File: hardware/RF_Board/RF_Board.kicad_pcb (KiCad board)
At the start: 4 copper layers, 90 x 90 mm, 130 parts, among them J1 Conn_Coaxial, J2 Conn_01x04_Male, J3 Conn_Coaxial, J4 Conn_01x04_Male, J5 Conn_01x06_Female, J6 Conn_01x06_Female, J7 Conn_01x06_Female, J8 L77TSAH15SOL2RM8, J9 Conn_01x09_Male, Q1 2N7002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

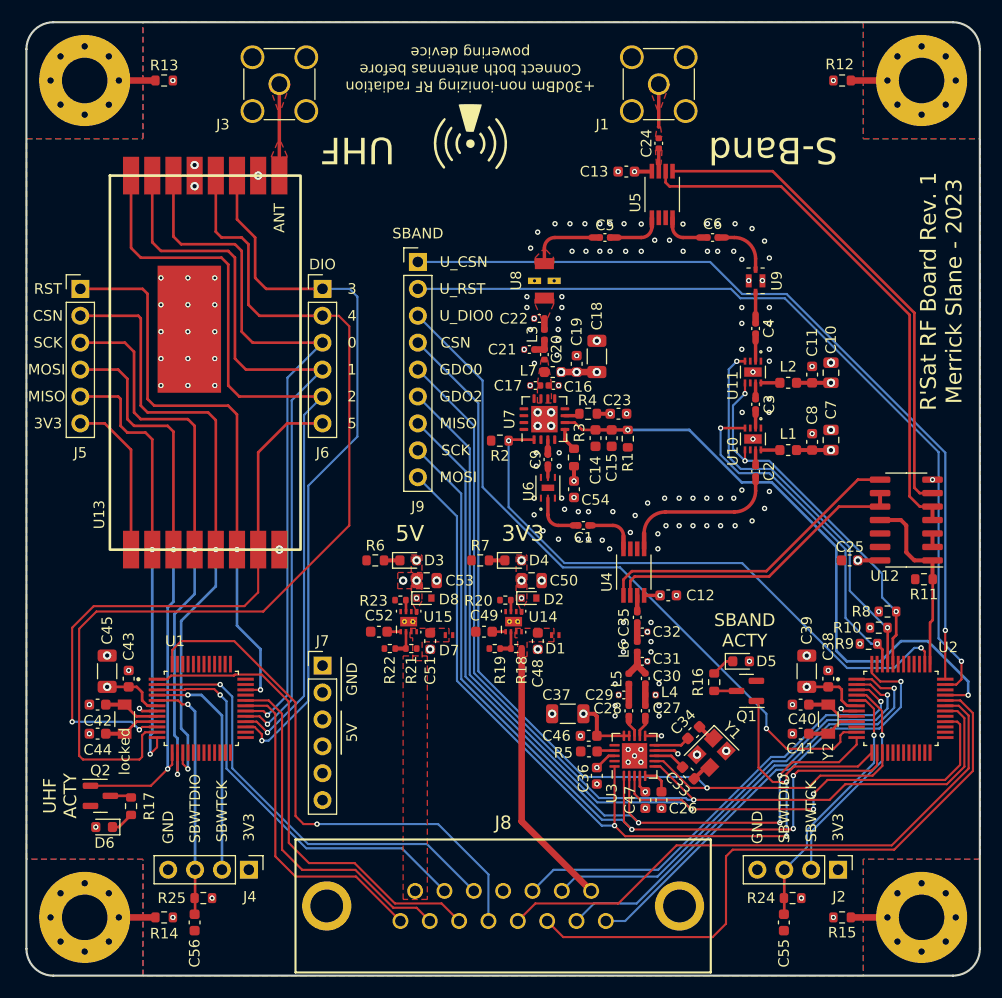
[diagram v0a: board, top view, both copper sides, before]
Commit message: respond to RF board feedback
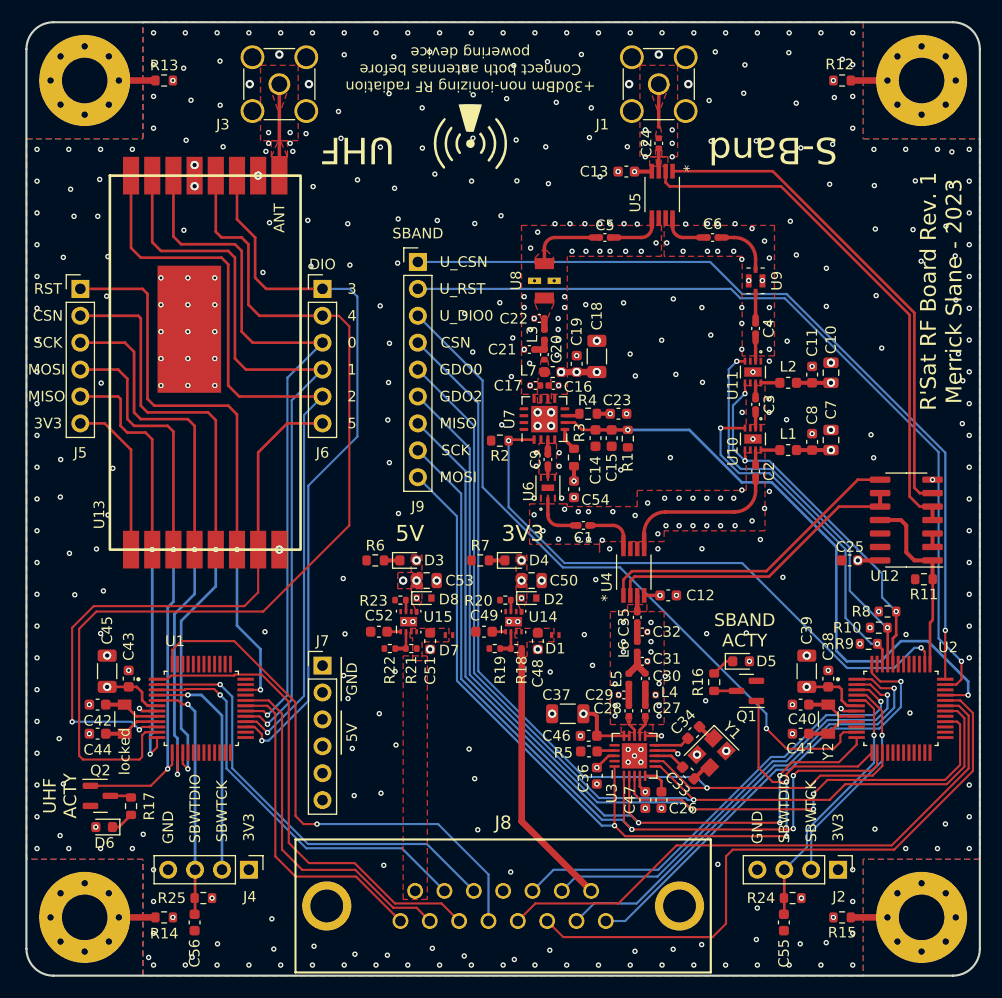
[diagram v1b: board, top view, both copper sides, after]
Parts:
- R3: value 24.9k -> 24.9
- R4: value 10k -> 10
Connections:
- U12 pad 13: unconnected-(U12-Pad13) -> GND
- U6 pad 7: (no net) -> GND
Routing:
- net GND: vias 173 -> 487
- added copper zone on F.Cu, net Net-(C27-Pad1)
- added copper zone on F.Cu, net Net-(C28-Pad1)

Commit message: Responded to all review items
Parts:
- U14, U15: value TPS259573DSGR -> DSG0008A
- U9: value DEA202450BT-1213C1 -> DEA-4_2P0X1P25
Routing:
- net /CC2500_UART_RX: track 59.6 -> 61.3 mm
- net GND: vias 487 -> 499

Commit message: final edits to RF Board, freezing further modifications before ordering
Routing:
- net GND: vias 499 -> 498
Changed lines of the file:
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@@
     (fp_line (start 1.6 -0.8) (end 1.6 0.8) (layer "F.Fab") (width 0.1))
     (fp_line (start 1.6 0.8) (end -1.6 0.8) (layer "F.Fab") (width 0.1))
-    (pad "1" smd roundrect locked (at -1.475 0 270) (size 1.15 1.8) (layers "F.Cu" "F.Paste" "F.Mask") (roundrect_rratio 0.217391)
+    (pad "1" smd roundrect locked (at -1.475 0 270) (size 1.15 1.8) (layers "F.Cu" "F.Paste" "F.Mask") (roundrect_rratio 0.2173913043)
       (net 13 "GND") (pintype "passive"))
-    (pad "2" smd roundrect locked (at 1.475 0 270) (size 1.15 1.8) (layers "F.Cu" "F.Paste" "F.Mask") (roundrect_rratio 0.217391)
+    (pad "2" smd roundrect locked (at 1.475 0 270) (size 1.15 1.8) (layers "F.Cu" "F.Paste" "F.Mask") (roundrect_rratio 0.2173913043)
       (net 22 "+3.3V") (pintype "passive"))
     (model "${KICAD6_3DMODEL_DIR}/Capacitor_SMD.3dshapes/C_1206_3216Metric.wrl"
@@
     (fp_line (start -2 -1) (end -1 -2) (layer "F.Fab") (width 0.1))
     (fp_line (start -2 2) (end -2 -1) (layer "F.Fab") (width 0.1))
-    (pad "" smd roundrect locked (at -0.625 0.625 90) (size 1.01 1.01) (layers "F.Paste") (roundrect_rratio 0.247525))
-    (pad "" smd roundrect locked (at -0.625 -0.625 90) (size 1.01 1.01) (layers "F.Paste") (roundrect_rratio 0.247525))
-    (pad "" smd roundrect locked (at 0.625 0.625 90) (size 1.01 1.01) (layers "F.Paste") (roundrect_rratio 0.247525))
-    (pad "" smd roundrect locked (at 0.625 -0.625 90) (size 1.01 1.01) (layers "F.Paste") (roundrect_rratio 0.247525))
+    (pad "" smd roundrect locked (at -0.625 0.625 90) (size 1.01 1.01) (layers "F.Paste") (roundrect_rratio 0.2475247525))
+    (pad "" smd roundrect locked (at -0.625 -0.625 90) (size 1.01 1.01) (layers "F.Paste") (roundrect_rratio 0.2475247525))
+    (pad "" smd roundrect locked (at 0.625 0.625 90) (size 1.01 1.01) (layers "F.Paste") (roundrect_rratio 0.2475247525))
+    (pad "" smd roundrect locked (at 0.625 -0.625 90) (size 1.01 1.01) (layers "F.Paste") (roundrect_rratio 0.2475247525))
     (pad "1" smd roundrect locked (at -1.9375 -0.975 90) (size 0.825 0.3) (layers "F.Cu" "F.Paste" "F.Mask") (roundrect_rratio 0.25)
       (net 91 "/PA_EN") (pinfunction "PA_EN") (pintype "input"))
@@
     (fp_line (start 1.6 0.8) (end -1.6 0.8) (layer "F.Fab") (width 0.1))
     (fp_line (start -1.6 -0.8) (end 1.6 -0.8) (layer "F.Fab") (width 0.1))
-    (pad "1" smd roundrect locked (at -1.475 0) (size 1.15 1.8) (layers "F.Cu" "F.Paste" "F.Mask") (roundrect_rratio 0.217391)
+    (pad "1" smd roundrect locked (at -1.475 0) (size 1.15 1.8) (layers "F.Cu" "F.Paste" "F.Mask") (roundrect_rratio 0.2173913043)
       (net 13 "GND") (pintype "passive"))
-    (pad "2" smd roundrect locked (at 1.475 0) (size 1.15 1.8) (layers "F.Cu" "F.Paste" "F.Mask") (roundrect_rratio 0.217391)
+    (pad "2" smd roundrect locked (at 1.475 0) (size 1.15 1.8) (layers "F.Cu" "F.Paste" "F.Mask") (roundrect_rratio 0.2173913043)
       (net 22 "+3.3V") (pintype "passive"))
     (model "${KICAD6_3DMODEL_DIR}/Capacitor_SMD.3dshapes/C_1206_3216Metric.wrl"
@@
     (fp_line (start 1.6 -0.8) (end 1.6 0.8) (layer "F.Fab") (width 0.1))
     (fp_line (start -1.6 -0.8) (end 1.6 -0.8) (layer "F.Fab") (width 0.1))
-    (pad "1" smd roundrect locked (at -1.475 0 90) (size 1.15 1.8) (layers "F.Cu" "F.Paste" "F.Mask") (roundrect_rratio 0.217391)
+    (pad "1" smd roundrect locked (at -1.475 0 90) (size 1.15 1.8) (layers "F.Cu" "F.Paste" "F.Mask") (roundrect_rratio 0.2173913043)
       (net 14 "+5V") (pintype "passive"))
-    (pad "2" smd roundrect locked (at 1.475 0 90) (size 1.15 1.8) (layers "F.Cu" "F.Paste" "F.Mask") (roundrect_rratio 0.217391)
+    (pad "2" smd roundrect locked (at 1.475 0 90) (size 1.15 1.8) (layers "F.Cu" "F.Paste" "F.Mask") (roundrect_rratio 0.2173913043)
       (net 13 "GND") (pintype "passive"))
     (model "${KICAD6_3DMODEL_DIR}/Capacitor_SMD.3dshapes/C_1206_3216Metric.wrl"
@@
     (fp_line (start -1.6 -0.8) (end 1.6 -0.8) (layer "F.Fab") (width 0.1))
     (fp_line (start 1.6 -0.8) (end 1.6 0.8) (layer "F.Fab") (width 0.1))
-    (pad "1" smd roundrect locked (at -1.475 0 270) (size 1.15 1.8) (layers "F.Cu" "F.Paste" "F.Mask") (roundrect_rratio 0.217391)
+    (pad "1" smd roundrect locked (at -1.475 0 270) (size 1.15 1.8) (layers "F.Cu" "F.Paste" "F.Mask") (roundrect_rratio 0.2173913043)
       (net 13 "GND") (pintype "passive"))
-    (pad "2" smd roundrect locked (at 1.475 0 270) (size 1.15 1.8) (layers "F.Cu" "F.Paste" "F.Mask") (roundrect_rratio 0.217391)
+    (pad "2" smd roundrect locked (at 1.475 0 270) (size 1.15 1.8) (layers "F.Cu" "F.Paste" "F.Mask") (roundrect_rratio 0.2173913043)
       (net 22 "+3.3V") (pintype "passive"))
     (model "${KICAD6_3DMODEL_DIR}/Capacitor_SMD.3dshapes/C_1206_3216Metric.wrl"
@@
   (via (at 69.477763 24.384) (size 0.508) (drill 0.254) (layers "F.Cu" "B.Cu") (net 13))
   (via (at 64.223599 47.528) (size 0.508) (drill 0.254) (layers "F.Cu" "B.Cu") (net 13))
-  (via (at 14.863248 19.633773) (size 0.508) (drill 0.254) (layers "F.Cu" "B.Cu") (free) (net 13))
   (via (at 80.098691 76.1635) (size 0.508) (drill 0.254) (layers "F.Cu" "B.Cu") (free) (net 13))
   (via (at 34.114524 37.541519) (size 0.508) (drill 0.254) (layers "F.Cu" "B.Cu") (free) (net 13))

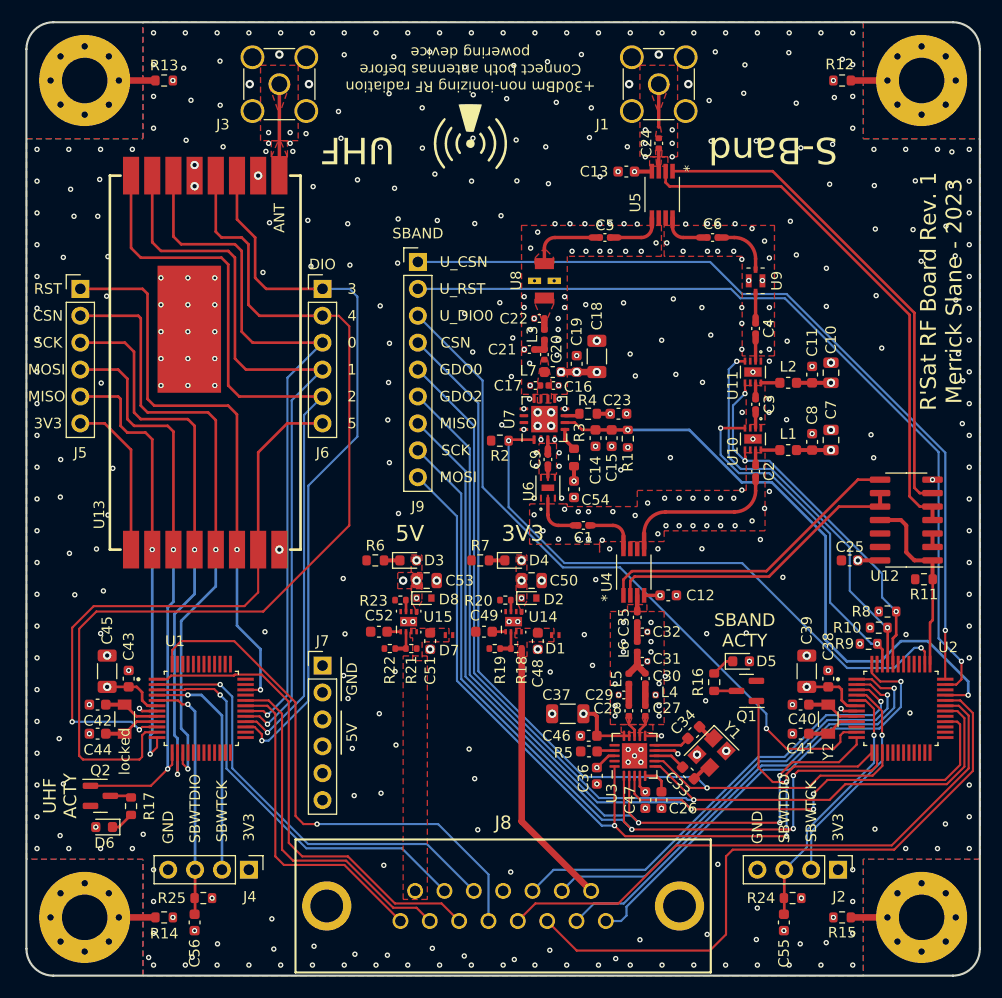
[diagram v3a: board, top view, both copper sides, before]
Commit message: update one footprint
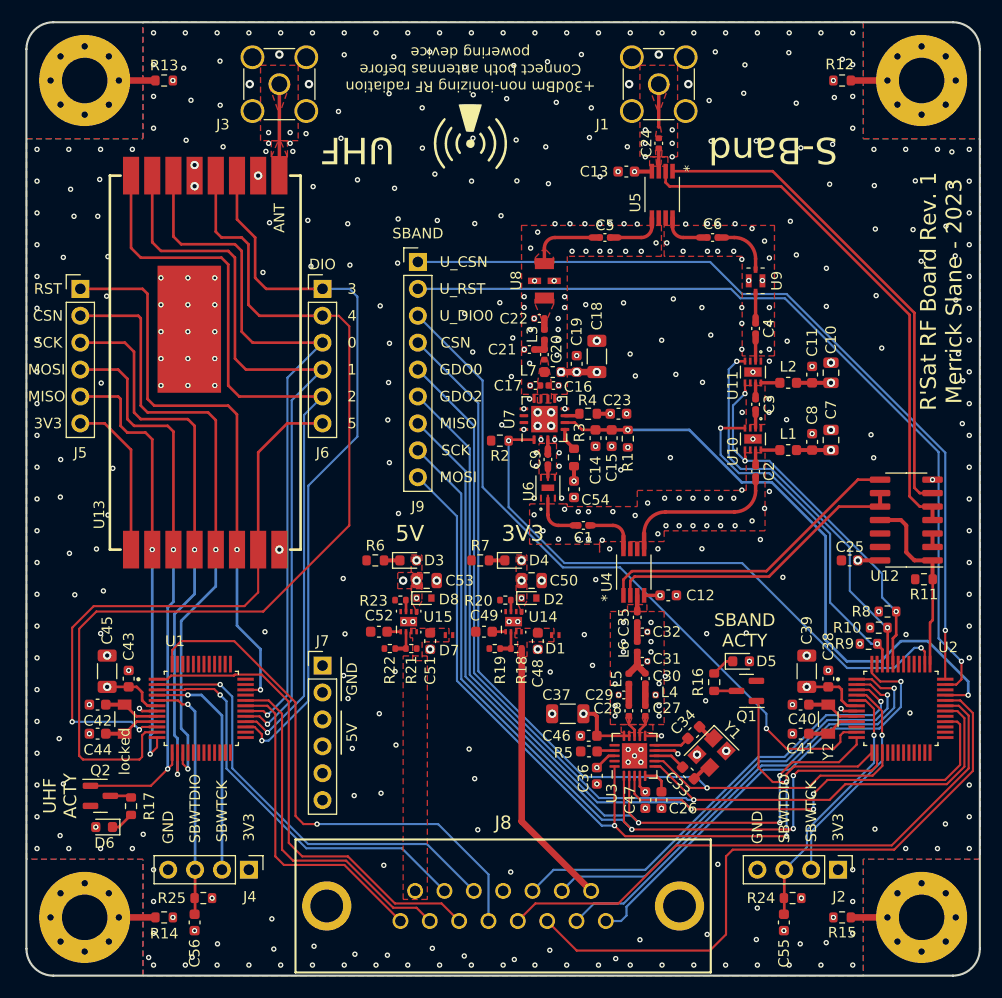
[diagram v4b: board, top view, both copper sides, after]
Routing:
- net GND: vias 498 -> 500
